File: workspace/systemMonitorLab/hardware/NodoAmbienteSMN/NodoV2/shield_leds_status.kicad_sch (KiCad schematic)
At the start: 4 parts, among them J7 Molex_Led_Status

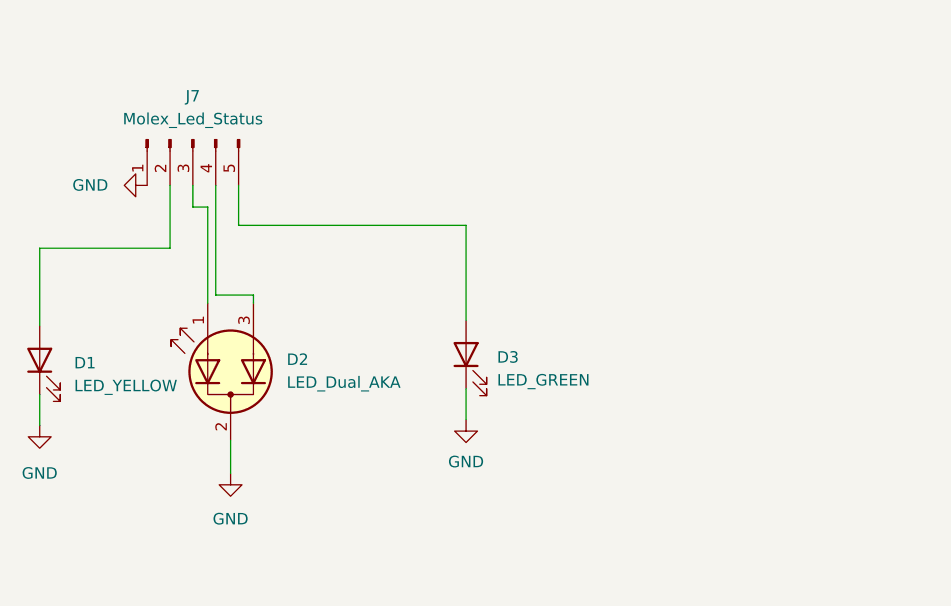
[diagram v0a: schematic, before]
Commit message: Se termino de generar el diseño de la placa shield_main_board.
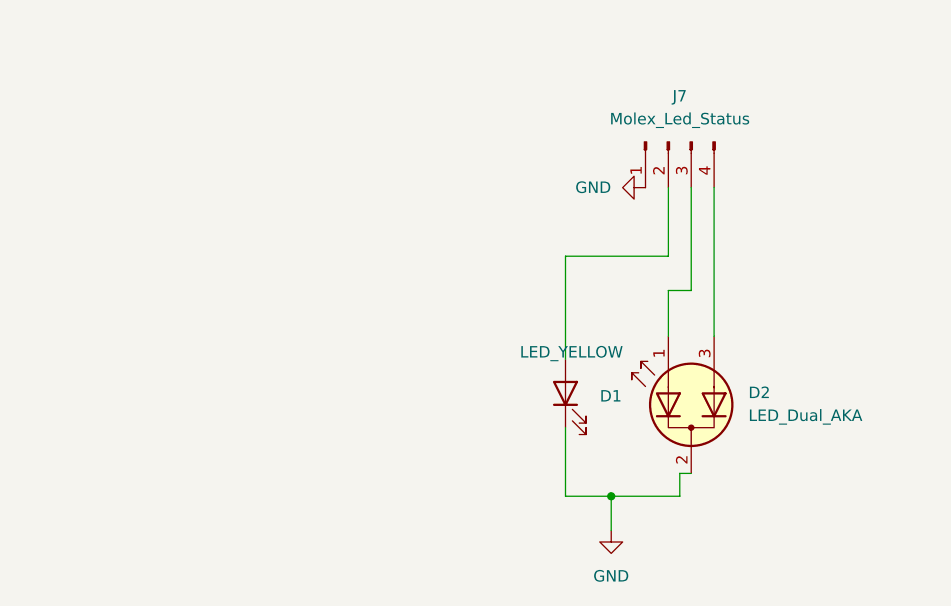
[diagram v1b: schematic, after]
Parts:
- removed D3: LED_GREEN, LED_THT:LED_D3.0mm, symbol Device:LED
- removed J7: Molex_Led_Status, Connector_PinHeader_2.54mm:PinHeader_1x05_P2.54mm_Horizontal, symbol Connector:Conn_01x05_Male
- added J7: Molex_Led_Status, Connector_PinHeader_2.54mm:PinHeader_1x04_P2.54mm_Horizontal, symbol Connector:Conn_01x04_Pin
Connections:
- net GND: now also J7.1 (Pin_1)
- net at D2.1 (A1): now also J7.3 (Pin_3)
- net at D2.3 (A2): now also J7.4 (Pin_4)
- net at D1.2 (A): now also J7.2 (Pin_2)
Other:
- company: (none) -> Servicio Meteorológico Nacional (SMN)
- title: (none) -> shield_leds_status_nodo

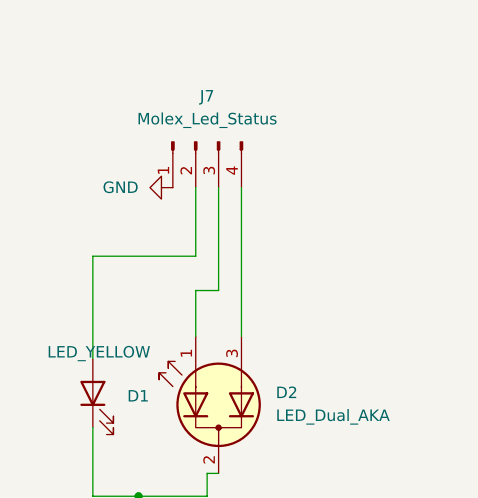
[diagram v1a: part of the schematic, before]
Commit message: Tareas Realizadas: 	- Se corrije la disposicion de los conectores, para que el cable 	  quede derecho en su construccion se tiene que invertir el 	  orden de los pines en las placas led_status y sensors. 	- Se Cambio el ancho de las pistas que atraviesan a los 	  resistores SMD de 30 a 25 mils. 	- Se esta transmitiendo al sevirdor nginx por el puerto 80. Tareas proximas: 	- Se debe Contruir las placas y realizar pruebas. 	- Modificar el firmware para que los led envien los estados por 	  PWM para el LED dual. y On - OFF para el Led simple. 	- Se debe agregar un filtro para que los datos que tengan una 	  varianza mayor a un valor x no se transmitan. 	- Se debe agregar un retardo para que no se transmitan los datos 	  de inicio del barometro, ya que siempre marcan un valor 	  alredeor de 700 hPa.
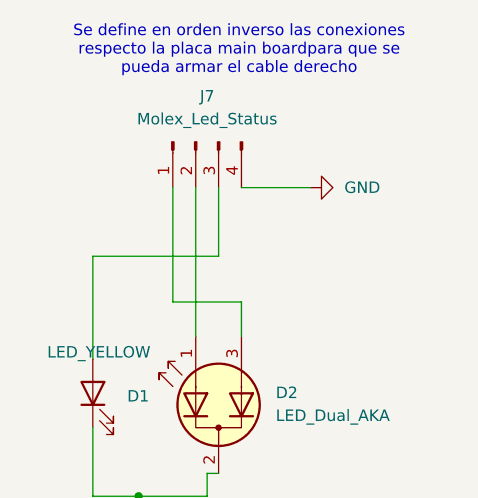
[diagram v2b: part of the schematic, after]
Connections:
- net GND: now also J7.4 (Pin_4); no longer J7.1 (Pin_1)
- net at J7.2 (Pin_2): now also D2.1 (A1); no longer D1.2 (A)
- net at J7.3 (Pin_3): now also D1.2 (A); no longer D2.1 (A1)
- net at D2.3 (A2): now also J7.1 (Pin_1); no longer J7.4 (Pin_4)
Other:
- note added: "Se define en orden inverso las conexiones respecto la placa main boardpara que se pueda armar el cable derecho"
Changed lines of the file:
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@@
 		(company "Servicio Meteorológico Nacional (SMN)")
+	)
+	(text "Se define en orden inverso las conexiones \nrespecto la placa main boardpara que se\npueda armar el cable derecho"
+		(exclude_from_sim no)
+		(at 192.786 49.53 0)
+		(effects
+			(font
+				(size 1.27 1.27)
+			)
+		)
 	)
 	(junction
@@
 	(wire
 		(pts
-			(xy 190.5 64.77) (xy 190.5 76.2)
+			(xy 176.53 72.39) (xy 190.5 72.39)
+		)
+		(stroke
+			(width 0)
+			(type default)
+		)
+	)
+	(wire
+		(pts
+			(xy 187.96 64.77) (xy 187.96 81.28)
+		)
+		(stroke
+			(width 0)
+			(type default)
+		)
+	)
+	(wire
+		(pts
+			(xy 193.04 64.77) (xy 200.66 64.77)
 		)
 		(stroke
@@
 	(wire
 		(pts
-			(xy 187.96 64.77) (xy 187.96 72.39)
-		)
-		(stroke
-			(width 0)
-			(type default)
-		)
-	)
-	(wire
-		(pts
 			(xy 176.53 91.44) (xy 176.53 99.06)
 		)
@@
 	(wire
 		(pts
-			(xy 187.96 76.2) (xy 187.96 81.28)
-		)
-		(stroke
-			(width 0)
-			(type default)
-		)
-	)
-	(wire
-		(pts
-			(xy 187.96 72.39) (xy 176.53 72.39)
-		)
-		(stroke
-			(width 0)
-			(type default)
-		)
-	)
-	(wire
-		(pts
-			(xy 190.5 76.2) (xy 187.96 76.2)
+			(xy 185.42 77.47) (xy 193.04 77.47)
+		)
+		(stroke
+			(width 0)
+			(type default)
+		)
+	)
+	(wire
+		(pts
+			(xy 193.04 77.47) (xy 193.04 81.28)
 		)
 		(stroke
@@
 	(wire
 		(pts
+			(xy 185.42 64.77) (xy 185.42 77.47)
+		)
+		(stroke
+			(width 0)
+			(type default)
+		)
+	)
+	(wire
+		(pts
 			(xy 176.53 72.39) (xy 176.53 83.82)
 		)
@@
 	(wire
 		(pts
-			(xy 193.04 64.77) (xy 193.04 81.28)
+			(xy 190.5 72.39) (xy 190.5 64.77)
 		)
 		(stroke
@@
 		(lib_name "GND_1")
 		(lib_id "power:GND")
-		(at 185.42 64.77 270)
+		(at 200.66 64.77 90)
 		(unit 1)
 		(exclude_from_sim no)
@@
 		(fields_autoplaced yes)
 		(property "Reference" "#PWR021"
-			(at 179.07 64.77 0)
+			(at 207.01 64.77 0)
 			(effects
 				(font
@@
 		)
 		(property "Value" "GND"
-			(at 181.61 64.7699 90)
+			(at 204.47 64.7699 90)
 			(effects
 				(font
@@
 		)
 		(property "Footprint" ""
-			(at 185.42 64.77 0)
+			(at 200.66 64.77 0)
 			(effects
 				(font
@@
 		)
 		(property "Datasheet" ""
-			(at 185.42 64.77 0)
+			(at 200.66 64.77 0)
 			(effects
 				(font
@@
 		)
 		(property "Description" "Power symbol creates a global label with name \"GND\" , ground"
-			(at 185.42 64.77 0)
-			(effects
-				(font
+			(at 200.66 64.77 0)
+			(effects
+				(font
